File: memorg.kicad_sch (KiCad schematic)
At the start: 8 parts, among them U76 MR25H40CDE, U77 MR25H40CDE, U78 MR25H40CDE, U79 MR25H40CDE

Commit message: Start ripping things apart
Signed-off-by: Corey Minyard <corey@minyard.net>
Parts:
- removed C77, C78, C79: 100n, Capacitor_SMD:C_0603_1608Metric_Pad1.08x0.95mm_HandSolder, symbol Device:C
- removed U76, U77, U78, U79: MR25H40CDE, PacSatDev_everspin:MR2xH40_DFN_SmallFlag, symbol PACSAT_ICs:MR25H40_2
- added U13: AS1016204-0108X0PWAY, Package_SON:WSON-8-1EP_8x6mm_P1.27mm_EP3.4x4.3mm, symbol LocalFlash:QSPI_FLASH_WSON_8-pin
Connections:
- net +3.3V: now also U13.3 (WP#/IO2), U13.7 (RST/IO3), U13.8 (VCC)
- net GND: now also U13.4 (GND), U13.9 (PAD)
- net MRAM_CLK: now also U13.6 (SCK)
- net MRAM_MISO: now also U13.2 (SO/IO1)
- net MRAM_MOSI: now also U13.5 (SI/IO0)
- net MRAM_NCS0: now also U13.1 (CS)
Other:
- note added: "MRAM 16 Mb 2MX8"
- note removed: "MRAM 4 Mb 512KX8"
- moved on the sheet: C76

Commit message: Do a lot of routing work
RX input is done, 5043s are done, power is done.

Signed-off-by: Corey Minyard <corey@minyard.net>
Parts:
- U13: symbol LocalFlash:QSPI_FLASH_WSON_8-pin -> PACSAT_ICs:QSPI_FLASH_WSON_8-pin
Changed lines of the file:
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@@
 	)
 	(symbol
-		(lib_id "LocalFlash:QSPI_FLASH_WSON_8-pin")
+		(lib_id "PACSAT_ICs:QSPI_FLASH_WSON_8-pin")
 		(at 82.55 49.53 0)
 		(unit 1)

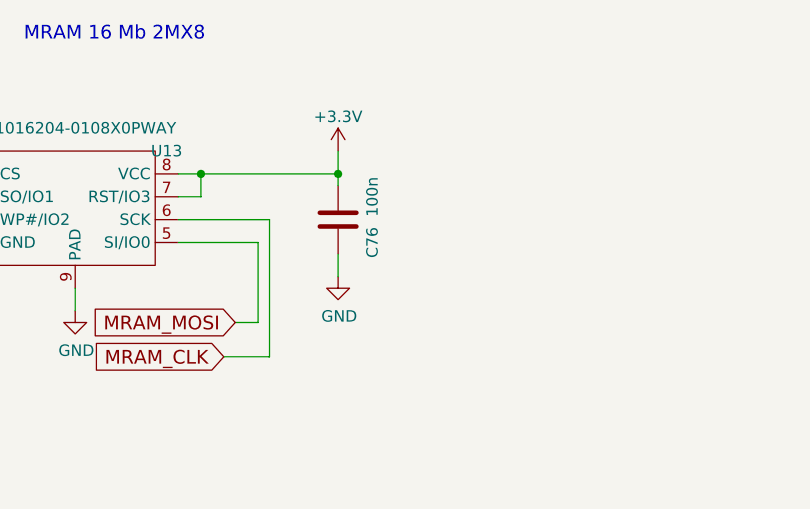
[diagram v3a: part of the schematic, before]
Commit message: Wire in clocks, more cleanups, wire in MRAM
Signed-off-by: Corey Minyard <corey@minyard.net>
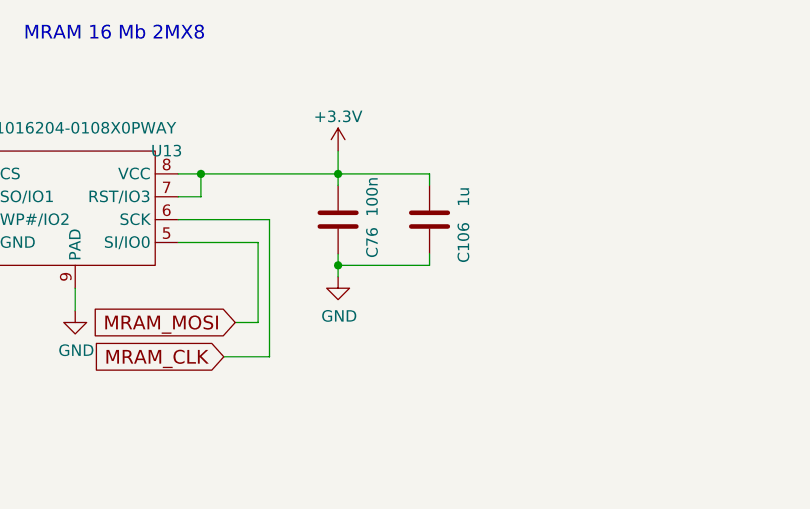
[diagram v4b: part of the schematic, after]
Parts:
- added C106: 1u, Capacitor_SMD:C_0603_1608Metric_Pad1.08x0.95mm_HandSolder, symbol Device:C
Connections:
- net +3.3V: now also C106.1
- net GND: now also C106.2
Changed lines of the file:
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@@
+	)
+	(junction
+		(at 111.76 55.88)
+		(diameter 0)
+		(color 0 0 0 0)
 	)
 	(junction
@@
 	(wire
 		(pts
+			(xy 121.92 46.99) (xy 121.92 45.72)
+		)
+		(stroke
+			(width 0)
+			(type default)
+		)
+	)
+	(wire
+		(pts
 			(xy 82.55 58.42) (xy 82.55 60.96)
 		)
@@
 	(wire
 		(pts
+			(xy 121.92 55.88) (xy 111.76 55.88)
+		)
+		(stroke
+			(width 0)
+			(type default)
+		)
+	)
+	(wire
+		(pts
 			(xy 71.12 50.8) (xy 68.58 50.8)
 		)
@@
 	(wire
 		(pts
+			(xy 121.92 45.72) (xy 111.76 45.72)
+		)
+		(stroke
+			(width 0)
+			(type default)
+		)
+	)
+	(wire
+		(pts
 			(xy 96.52 48.26) (xy 96.52 45.72)
 		)
@@
 	(wire
 		(pts
+			(xy 111.76 55.88) (xy 111.76 57.15)
+		)
+		(stroke
+			(width 0)
+			(type default)
+		)
+	)
+	(wire
+		(pts
 			(xy 71.12 53.34) (xy 68.58 53.34)
 		)
@@
 	(wire
 		(pts
+			(xy 121.92 54.61) (xy 121.92 55.88)
+		)
+		(stroke
+			(width 0)
+			(type default)
+		)
+	)
+	(wire
+		(pts
 			(xy 111.76 45.72) (xy 111.76 46.99)
 		)
@@
 	(wire
 		(pts
-			(xy 111.76 54.61) (xy 111.76 57.15)
+			(xy 111.76 54.61) (xy 111.76 55.88)
 		)
 		(stroke
@@
 					(unit 1)
 				)
+			)
+		)
+	)
+	(symbol
+		(lib_id "Device:C")
+		(at 121.92 50.8 0)
+		(unit 1)
+		(exclude_from_sim no)
+		(in_bom yes)
+		(on_board yes)
+		(dnp no)
+		(property "Reference" "C106"
+			(at 125.73 53.34 90)
+			(effects
+				(font
+					(size 1.27 1.27)
+				)
+			)
+		)
+		(property "Value" "1u"
+			(at 125.73 48.26 90)
+			(effects
+				(font
+					(size 1.27 1.27)
+				)
+			)
+		)
+		(property "Footprint" "Capacitor_SMD:C_0603_1608Metric_Pad1.08x0.95mm_HandSolder"
+			(at 122.8852 54.61 0)
+			(effects
+				(font
+					(size 1.27 1.27)
+				)
+				(hide yes)
+			)
+		)
+		(property "Datasheet" "~"
+			(at 121.92 50.8 0)
+			(effects
+				(font
+					(size 1.27 1.27)
+				)
+			)
+		)
+		(property "Description" ""
+			(at 121.92 50.8 0)
+			(effects
+				(font
+					(size 1.27 1.27)
+				)
+			)
+		)
+		(pin "1"
+		)
+		(pin "2"
+		)
+		(instances
+			(project "PacSat_AFSK"
+				(path "/cc9f42d2-6985-41ac-acab-5ab7b01c5b38/552b793d-9664-4666-9fdb-015ae3bc3958"
+					(reference "C106")
+					(unit 1)
+				)

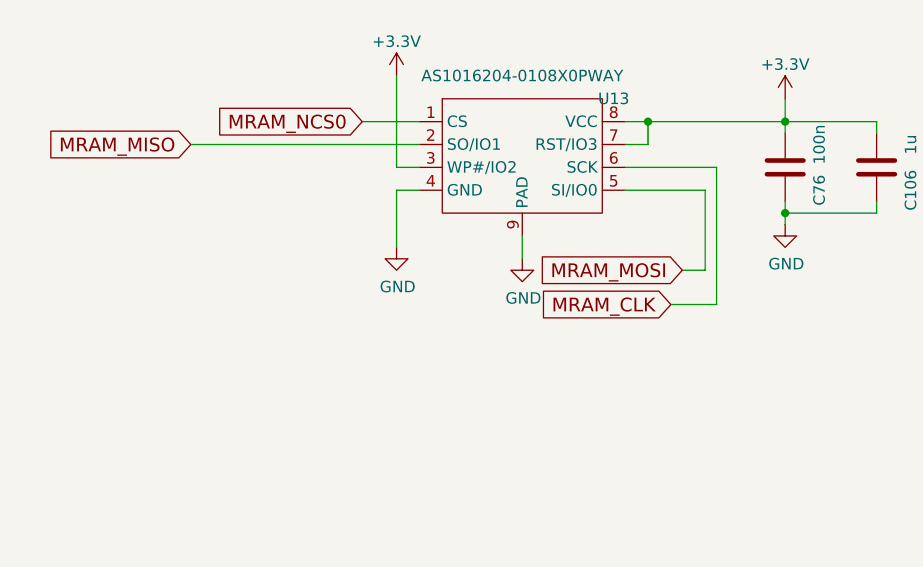
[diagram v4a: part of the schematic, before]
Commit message: Add resistors to the JTAG interface
They are supposed to be there.

Signed-off-by: Corey Minyard <corey@minyard.net>
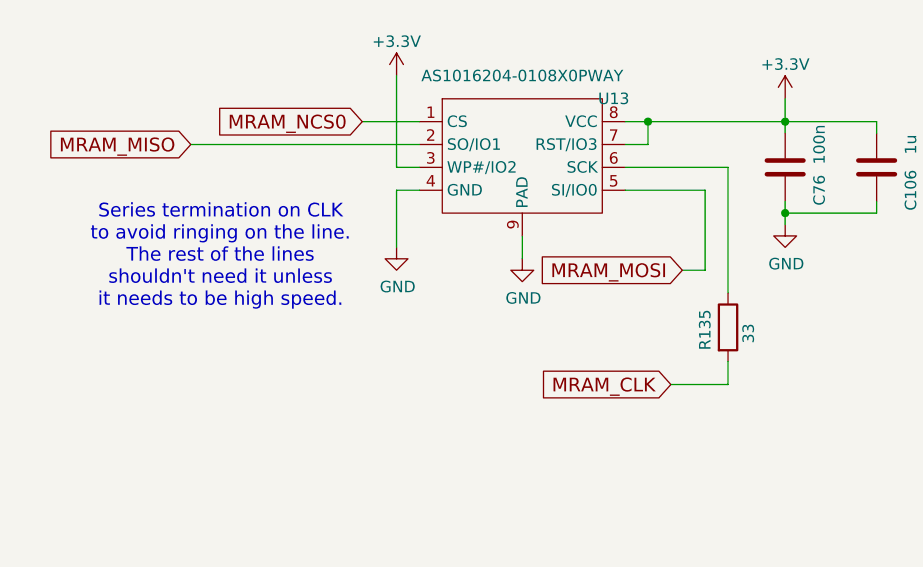
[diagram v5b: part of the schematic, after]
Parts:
- added R135: 33, Resistor_SMD:R_0603_1608Metric_Pad0.98x0.95mm_HandSolder, symbol Device:R
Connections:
- net MRAM_CLK: now also R135.2; no longer U13.6 (SCK)
- new net: R135.1, U13.6 (SCK)
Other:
- note added: "Series termination on CLK to avoid ringing on the line. The rest of the lines shouldn't need it unless it needs to be high speed."
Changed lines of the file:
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@@
+		)
+	)
+	(text "Series termination on CLK\nto avoid ringing on the line.\nThe rest of the lines\nshouldn't need it unless\nit needs to be high speed."
+		(exclude_from_sim no)
+		(at 49.022 60.706 0)
+		(effects
+			(font
+				(size 1.524 1.524)
+			)
 		)
 	)
@@
 	(wire
 		(pts
-			(xy 104.14 66.04) (xy 99.06 66.04)
+			(xy 105.41 74.93) (xy 99.06 74.93)
 		)
 		(stroke
@@
 	(wire
 		(pts
-			(xy 104.14 50.8) (xy 104.14 66.04)
+			(xy 105.41 50.8) (xy 105.41 64.77)
+		)
+		(stroke
+			(width 0)
+			(type default)
+		)
+	)
+	(wire
+		(pts
+			(xy 105.41 72.39) (xy 105.41 74.93)
 		)
 		(stroke
@@
 	(wire
 		(pts
-			(xy 104.14 50.8) (xy 93.98 50.8)
+			(xy 105.41 50.8) (xy 93.98 50.8)
 		)
 		(stroke
@@
 	(global_label "MRAM_CLK"
 		(shape input)
-		(at 99.06 66.04 180)
+		(at 99.06 74.93 180)
 		(fields_autoplaced yes)
 		(effects
@@
 		)
 		(property "Intersheetrefs" "${INTERSHEET_REFS}"
-			(at 84.6021 66.04 0)
+			(at 84.6021 74.93 0)
 			(effects
 				(font
@@
 			)
 		)
+	)
+	(symbol
+		(lib_id "Device:R")
+		(at 105.41 68.58 0)
+		(unit 1)
+		(exclude_from_sim no)
+		(in_bom yes)
+		(on_board yes)
+		(dnp no)
+		(property "Reference" "R135"
+			(at 102.87 71.12 90)
+			(effects
+				(font
+					(size 1.27 1.27)
+				)
+				(justify left)
+			)
+		)
+		(property "Value" "33"
+			(at 107.696 70.358 90)
+			(effects
+				(font
+					(size 1.27 1.27)
+				)
+				(justify left)
+			)
+		)
+		(property "Footprint" "Resistor_SMD:R_0603_1608Metric_Pad0.98x0.95mm_HandSolder"
+			(at 103.632 68.58 90)
+			(effects
+				(font
+					(size 1.27 1.27)
+				)
+				(hide yes)
+			)
+		)
+		(property "Datasheet" "~"
+			(at 105.41 68.58 0)
+			(effects
+				(font
+					(size 1.27 1.27)
+				)
+			)
+		)
+		(property "Description" ""
+			(at 105.41 68.58 0)
+			(effects
+				(font
+					(size 1.27 1.27)
+				)
+			)
+		)
+		(pin "1"
+		)
+		(pin "2"
+		)
+		(instances
+			(project "PacSat_AFSK"
+				(path "/cc9f42d2-6985-41ac-acab-5ab7b01c5b38/552b793d-9664-4666-9fdb-015ae3bc3958"
+					(reference "R135")
+					(unit 1)
+				)
+			)
+		)
